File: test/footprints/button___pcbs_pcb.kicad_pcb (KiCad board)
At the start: 2 copper layers, 2 parts

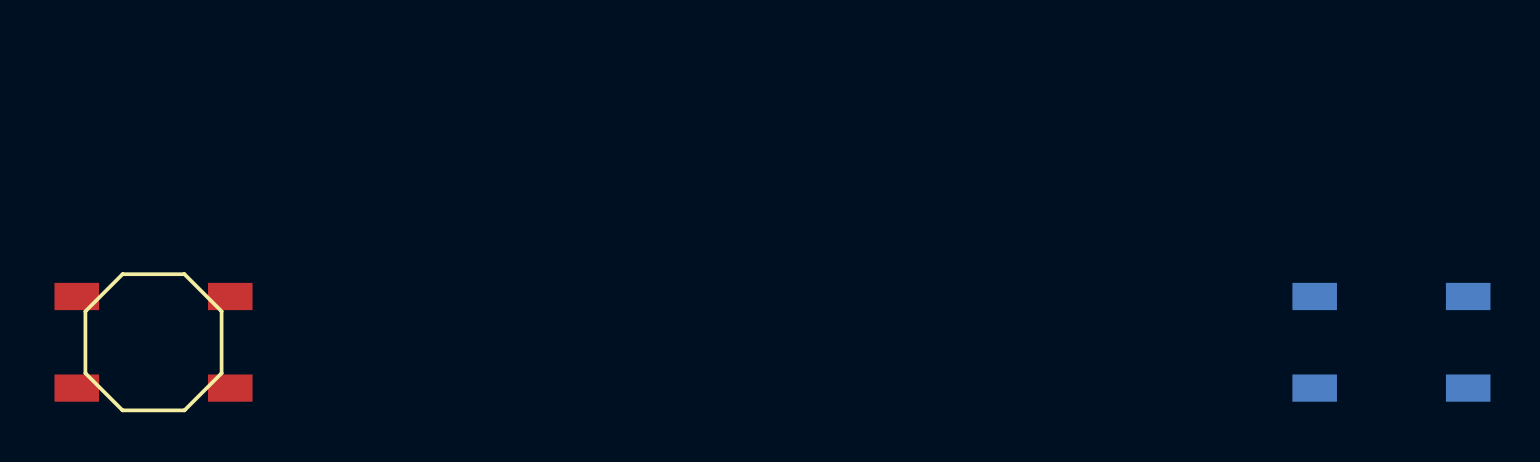
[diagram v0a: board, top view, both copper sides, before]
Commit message: Add PTS636_SK43_LFS variant for button
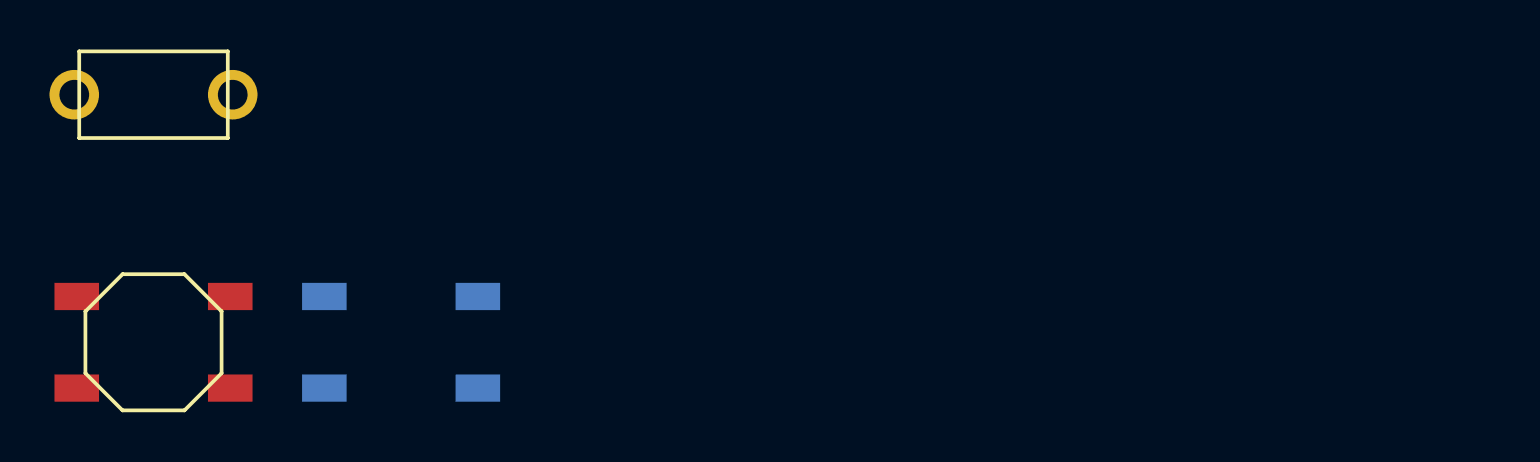
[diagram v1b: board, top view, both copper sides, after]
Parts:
- added B3: , SW_TACT_PTS636_SK43_LFS, F.Cu at (0.00, -10.0)
- moved B2 40.0 mm to (10.0, 0.00)
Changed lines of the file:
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@@
   )
     (module E73:SW_TACT_ALPS_SKQGABE010 (layer F.Cu)
-        (descr "Low-profile SMD Tactile Switch, https://www.e-switch.com/product-catalog/tact/product-lines/tl3342-series-low-profile-smt-tact-switch")
-        (tags "SPST Tactile Switch")
-        (at 0 0 0)
-        (fp_text reference "B1" (at 0 0) (layer F.SilkS) hide (effects (font (size 1.27 1.27) (thickness 0.15))))
-        (fp_text value "" (at 0 0) (layer F.SilkS) hide (effects (font (size 1.27 1.27) (thickness 0.15))))
-        (fp_line (start 2.75 1.25) (end 1.25 2.75) (layer F.SilkS) (width 0.15))
-        (fp_line (start 2.75 -1.25) (end 1.25 -2.75) (layer F.SilkS) (width 0.15))
-        (fp_line (start 2.75 -1.25) (end 2.75 1.25) (layer F.SilkS) (width 0.15))
-        (fp_line (start -1.25 2.75) (end 1.25 2.75) (layer F.SilkS) (width 0.15))
-        (fp_line (start -1.25 -2.75) (end 1.25 -2.75) (layer F.SilkS) (width 0.15))
-        (fp_line (start -2.75 1.25) (end -1.25 2.75) (layer F.SilkS) (width 0.15))
-        (fp_line (start -2.75 -1.25) (end -1.25 -2.75) (layer F.SilkS) (width 0.15))
-        (fp_line (start -2.75 -1.25) (end -2.75 1.25) (layer F.SilkS) (width 0.15))
-        (pad 1 smd rect (at -3.1 -1.85 0) (size 1.8 1.1) (layers F.Cu F.Paste F.Mask) (net 1 "from"))
-        (pad 1 smd rect (at 3.1 -1.85 0) (size 1.8 1.1) (layers F.Cu F.Paste F.Mask) (net 1 "from"))
-        (pad 2 smd rect (at -3.1 1.85 0) (size 1.8 1.1) (layers F.Cu F.Paste F.Mask) (net 2 "to"))
-        (pad 2 smd rect (at 3.1 1.85 0) (size 1.8 1.1) (layers F.Cu F.Paste F.Mask) (net 2 "to"))
+      (descr "Low-profile SMD Tactile Switch, https://www.e-switch.com/product-catalog/tact/product-lines/tl3342-series-low-profile-smt-tact-switch")
+      (tags "SPST Tactile Switch")
+      (at 0 0 0)
+      (fp_text reference "B1" (at 0 0) (layer F.SilkS) hide (effects (font (size 1.27 1.27) (thickness 0.15))))
+      (fp_text value "" (at 0 0) (layer F.SilkS) hide (effects (font (size 1.27 1.27) (thickness 0.15))))
+      (fp_line (start 2.75 1.25) (end 1.25 2.75) (layer F.SilkS) (width 0.15))
+      (fp_line (start 2.75 -1.25) (end 1.25 -2.75) (layer F.SilkS) (width 0.15))
+      (fp_line (start 2.75 -1.25) (end 2.75 1.25) (layer F.SilkS) (width 0.15))
+      (fp_line (start -1.25 2.75) (end 1.25 2.75) (layer F.SilkS) (width 0.15))
+      (fp_line (start -1.25 -2.75) (end 1.25 -2.75) (layer F.SilkS) (width 0.15))
+      (fp_line (start -2.75 1.25) (end -1.25 2.75) (layer F.SilkS) (width 0.15))
+      (fp_line (start -2.75 -1.25) (end -1.25 -2.75) (layer F.SilkS) (width 0.15))
+      (fp_line (start -2.75 -1.25) (end -2.75 1.25) (layer F.SilkS) (width 0.15))
+      (pad 1 smd rect (at -3.1 -1.85 0) (size 1.8 1.1) (layers F.Cu F.Paste F.Mask) (net 1 "from"))
+      (pad 1 smd rect (at 3.1 -1.85 0) (size 1.8 1.1) (layers F.Cu F.Paste F.Mask) (net 1 "from"))
+      (pad 2 smd rect (at -3.1 1.85 0) (size 1.8 1.1) (layers F.Cu F.Paste F.Mask) (net 2 "to"))
+      (pad 2 smd rect (at 3.1 1.85 0) (size 1.8 1.1) (layers F.Cu F.Paste F.Mask) (net 2 "to"))
     )
     (module E73:SW_TACT_ALPS_SKQGABE010 (layer F.Cu)
-        (descr "Low-profile SMD Tactile Switch, https://www.e-switch.com/product-catalog/tact/product-lines/tl3342-series-low-profile-smt-tact-switch")
-        (tags "SPST Tactile Switch")
-        (at 50 0 0)
-        (fp_text reference "B2" (at 0 0) (layer F.SilkS) hide (effects (font (size 1.27 1.27) (thickness 0.15))))
-        (fp_text value "" (at 0 0) (layer F.SilkS) hide (effects (font (size 1.27 1.27) (thickness 0.15))))
-        (fp_line (start 2.75 1.25) (end 1.25 2.75) (layer B.SilkS) (width 0.15))
-        (fp_line (start 2.75 -1.25) (end 1.25 -2.75) (layer B.SilkS) (width 0.15))
-        (fp_line (start 2.75 -1.25) (end 2.75 1.25) (layer B.SilkS) (width 0.15))
-        (fp_line (start -1.25 2.75) (end 1.25 2.75) (layer B.SilkS) (width 0.15))
-        (fp_line (start -1.25 -2.75) (end 1.25 -2.75) (layer B.SilkS) (width 0.15))
-        (fp_line (start -2.75 1.25) (end -1.25 2.75) (layer B.SilkS) (width 0.15))
-        (fp_line (start -2.75 -1.25) (end -1.25 -2.75) (layer B.SilkS) (width 0.15))
-        (fp_line (start -2.75 -1.25) (end -2.75 1.25) (layer B.SilkS) (width 0.15))
-        (pad 1 smd rect (at -3.1 -1.85 0) (size 1.8 1.1) (layers B.Cu B.Paste B.Mask) (net 1 "from"))
-        (pad 1 smd rect (at 3.1 -1.85 0) (size 1.8 1.1) (layers B.Cu B.Paste B.Mask) (net 1 "from"))
-        (pad 2 smd rect (at -3.1 1.85 0) (size 1.8 1.1) (layers B.Cu B.Paste B.Mask) (net 2 "to"))
-        (pad 2 smd rect (at 3.1 1.85 0) (size 1.8 1.1) (layers B.Cu B.Paste B.Mask) (net 2 "to"))
+      (descr "Low-profile SMD Tactile Switch, https://www.e-switch.com/product-catalog/tact/product-lines/tl3342-series-low-profile-smt-tact-switch")
+      (tags "SPST Tactile Switch")
+      (at 10 0 0)
+      (fp_text reference "B2" (at 0 0) (layer F.SilkS) hide (effects (font (size 1.27 1.27) (thickness 0.15))))
+      (fp_text value "" (at 0 0) (layer F.SilkS) hide (effects (font (size 1.27 1.27) (thickness 0.15))))
+      (fp_line (start 2.75 1.25) (end 1.25 2.75) (layer B.SilkS) (width 0.15))
+      (fp_line (start 2.75 -1.25) (end 1.25 -2.75) (layer B.SilkS) (width 0.15))
+      (fp_line (start 2.75 -1.25) (end 2.75 1.25) (layer B.SilkS) (width 0.15))
+      (fp_line (start -1.25 2.75) (end 1.25 2.75) (layer B.SilkS) (width 0.15))
+      (fp_line (start -1.25 -2.75) (end 1.25 -2.75) (layer B.SilkS) (width 0.15))
+      (fp_line (start -2.75 1.25) (end -1.25 2.75) (layer B.SilkS) (width 0.15))
+      (fp_line (start -2.75 -1.25) (end -1.25 -2.75) (layer B.SilkS) (width 0.15))
+      (fp_line (start -2.75 -1.25) (end -2.75 1.25) (layer B.SilkS) (width 0.15))
+      (pad 1 smd rect (at -3.1 -1.85 0) (size 1.8 1.1) (layers B.Cu B.Paste B.Mask) (net 1 "from"))
+      (pad 1 smd rect (at 3.1 -1.85 0) (size 1.8 1.1) (layers B.Cu B.Paste B.Mask) (net 1 "from"))
+      (pad 2 smd rect (at -3.1 1.85 0) (size 1.8 1.1) (layers B.Cu B.Paste B.Mask) (net 2 "to"))
+      (pad 2 smd rect (at 3.1 1.85 0) (size 1.8 1.1) (layers B.Cu B.Paste B.Mask) (net 2 "to"))
+    )
+    (module SW_TACT_PTS636_SK43_LFS (layer F.Cu)
+      (descr "THT Tactile Switch, https://www.ckswitches.com/media/2779/pts636.pdf")
+      (tags "THT Tactile Switch")
+      (at 0 -10 0)
+      (fp_text reference "B3" (at 0 0) (layer F.SilkS) hide (effects (font (size 1.27 1.27) (thickness 0.15))))
+      (fp_text value "" (at 0 0) (layer F.SilkS) hide (effects (font (size 1.27 1.27) (thickness 0.15))))
+      (fp_line (start -3 -1.75) (end 3 -1.75) (layer F.SilkS) (width 0.15))
+      (fp_line (start 3 -1.75) (end 3 1.75) (layer F.SilkS) (width 0.15))
+      (fp_line (start 3 1.75) (end -3 1.75) (layer F.SilkS) (width 0.15))
+      (fp_line (start -3 1.75) (end -3 -1.75) (layer F.SilkS) (width 0.15))
+      (pad 1 thru_hole circle (at 3.2 0 0) (size 2 2) (drill 1.2) (layers *.Cu *.Mask) (net 1 "from"))
+      (pad 2 thru_hole circle (at -3.2 0 0) (size 2 2) (drill 1.2) (layers *.Cu *.Mask) (net 2 "to"))
     )
 )
